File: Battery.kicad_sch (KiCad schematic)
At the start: 12 parts

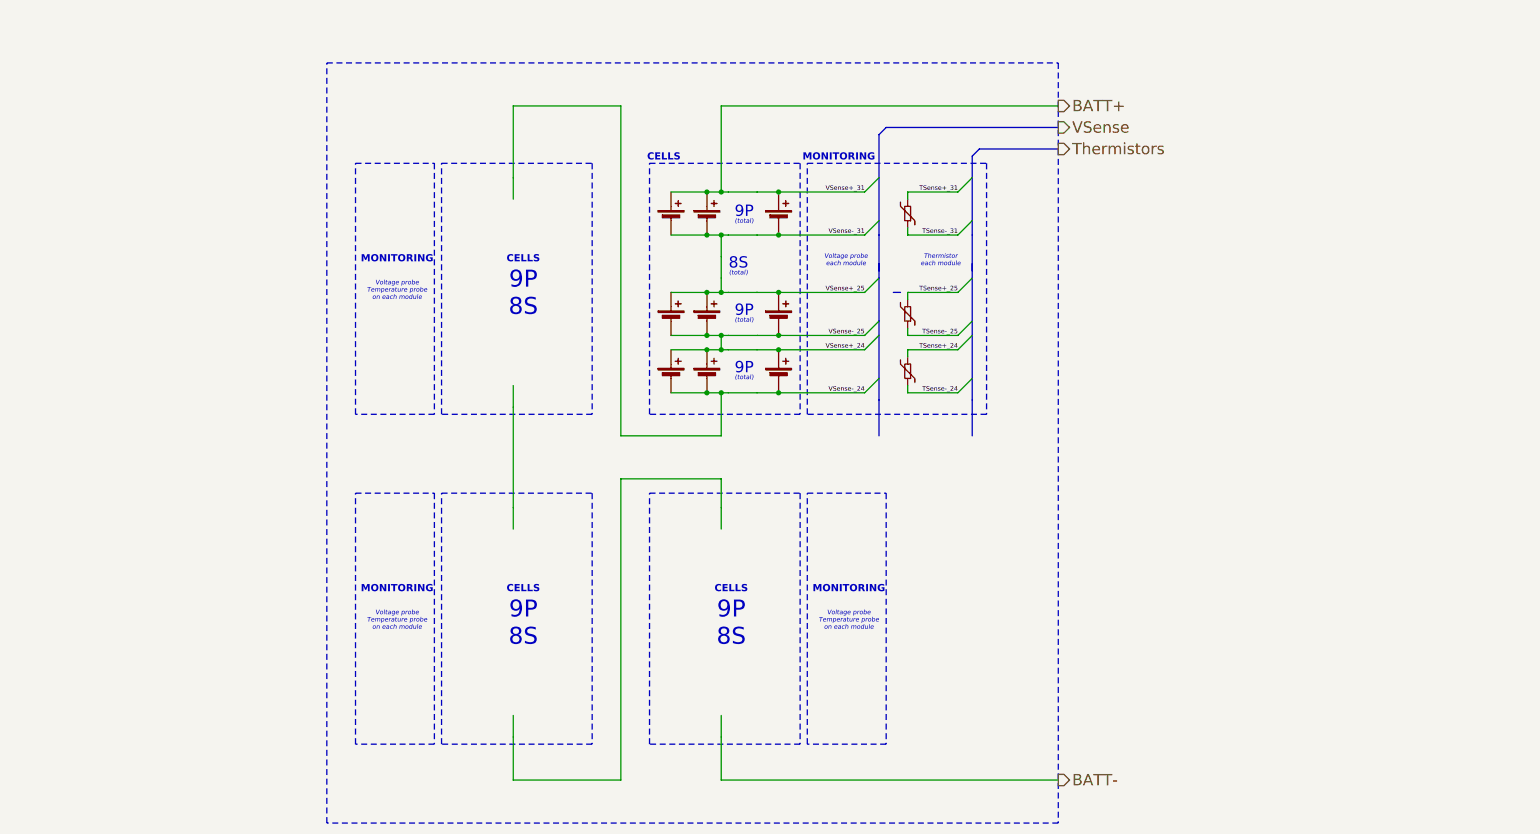
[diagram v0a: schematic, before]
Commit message: reorganized top
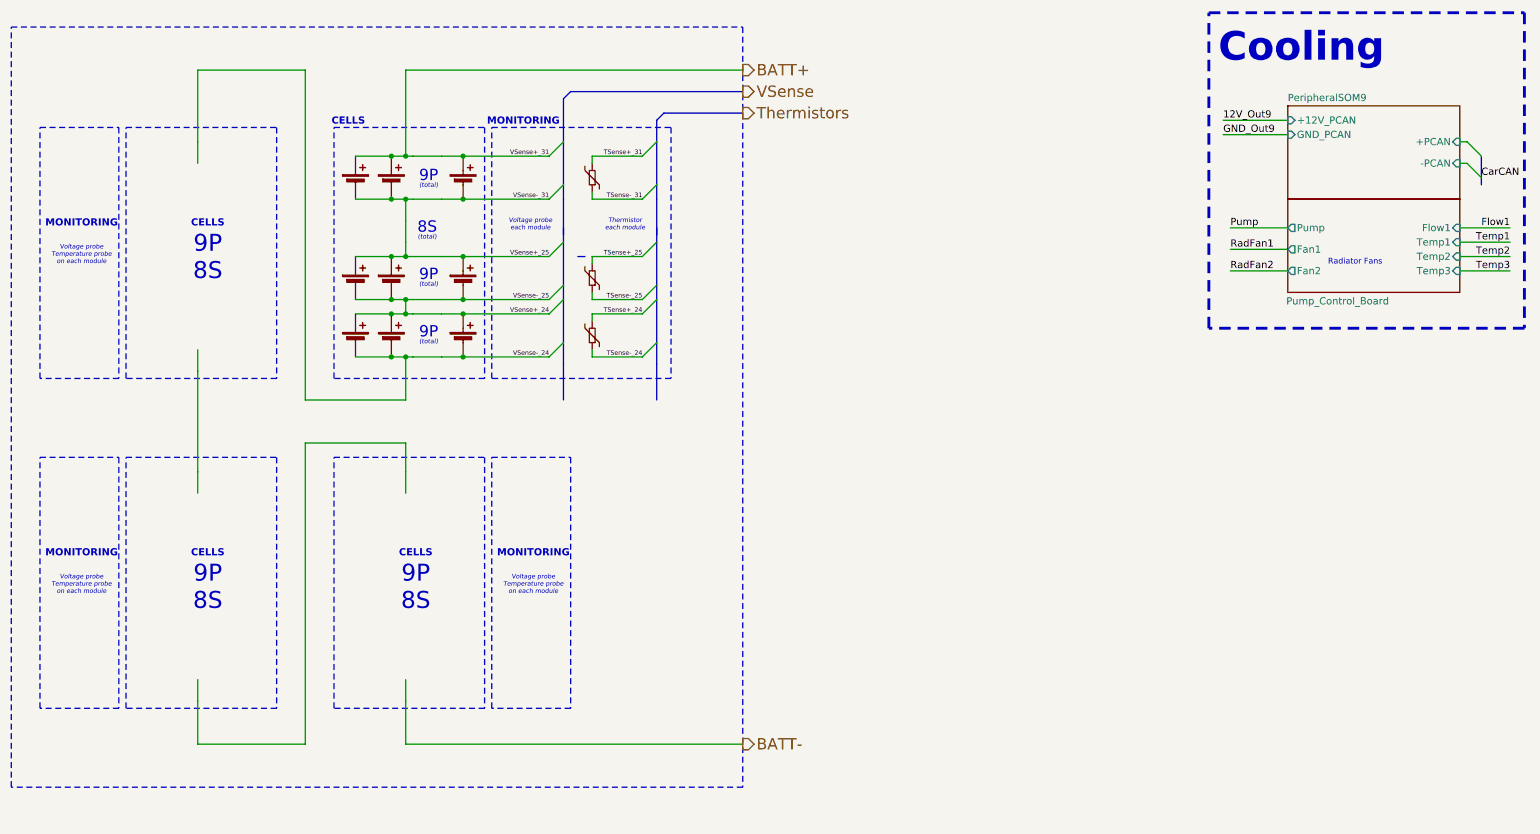
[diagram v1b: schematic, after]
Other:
- added sheet PeripheralSOM9 (PeripheralSOM.kicad_sch)
- added sheet Pump_Control_Board (Pump_Control_Board.kicad_sch)
- note added: "Cooling"
- note added: "Radiator Fans"

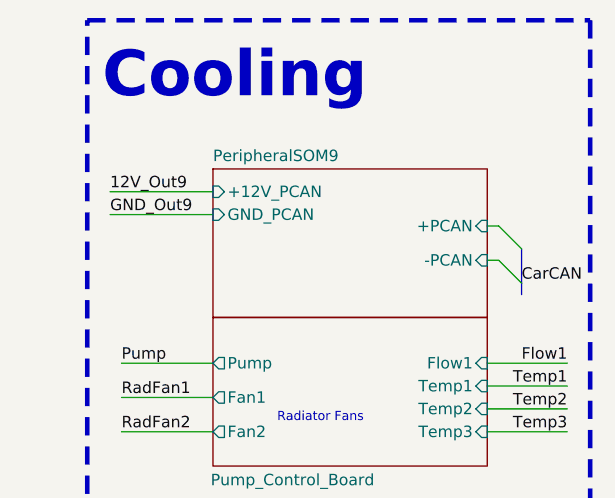
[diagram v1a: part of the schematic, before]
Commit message: Updated Controls + Telemetry
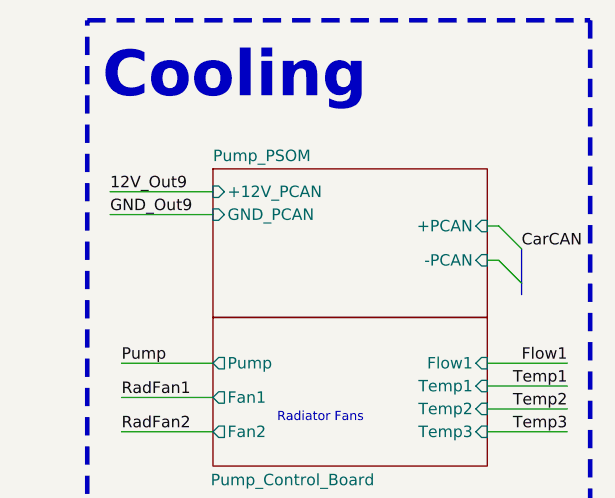
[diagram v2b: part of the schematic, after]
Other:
- sheet PeripheralSOM9 renamed Pump_PSOM
